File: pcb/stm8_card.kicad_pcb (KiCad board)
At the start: 2 copper layers, 101.9 x 50.9 mm, 22 parts, among them J1 DEBUG HEADER, SW1 TL59AF100Q, SW2 TL59AF100Q, SW3 TL59AF100Q, SW4 TL3302AF260QG, U1 ER-OLED0.91-7, U2 STM8S103F3

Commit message: pcb small edits
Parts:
- moved C8 2.00 mm to (261.5, 107.0)
- moved R1 2.00 mm to (229.0, 107.0)
- moved R3 2.00 mm to (251.5, 107.0)
- moved R4 2.00 mm to (254.0, 107.0), turned to 270 degrees
- moved R5 2.00 mm to (256.5, 107.0)
- moved R6 2.00 mm to (259.0, 107.0)
- moved C1 1.50 mm to (246.5, 107.0)
- moved C7 1.50 mm to (231.5, 107.0)
- moved R2 1.50 mm to (249.0, 107.0)
- moved C2 1.00 mm to (244.0, 107.0)
- moved C6 1.00 mm to (234.0, 107.0)
- moved C3 0.50 mm to (241.5, 107.0)
- moved C5 0.50 mm to (236.5, 107.0)
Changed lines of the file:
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@@
   )
   (module Capacitor_SMD:C_0805_2012Metric_Pad1.18x1.45mm_HandSolder (layer F.Cu)
-    (at 248 106.9625 90)
+    (at 246.5 107 90)
     (descr "Capacitor SMD 0805 (2012 Metric), square (rectangular) end terminal, IPC_7351 nominal with elongated pad for handsoldering. (Body size source: IPC-SM-782 page 76, https://www.pcb-3d.com/wordpress/wp-content/uploads/ipc-sm-782a_amendment_1_and_2.pdf, https://docs.google.com/spreadsheets/d/1BsfQQcO9C6DZCsRaXUlFlo91Tg2WpOkGARC1WS5S8t0/edit?usp=sharing), generated with kicad-footprint-generator")
     (tags "capacitor handsolder")
@@
   )
   (module Capacitor_SMD:C_0805_2012Metric_Pad1.18x1.45mm_HandSolder (layer F.Cu)
-    (at 245 106.9625 90)
+    (at 244 107 90)
     (descr "Capacitor SMD 0805 (2012 Metric), square (rectangular) end terminal, IPC_7351 nominal with elongated pad for handsoldering. (Body size source: IPC-SM-782 page 76, https://www.pcb-3d.com/wordpress/wp-content/uploads/ipc-sm-782a_amendment_1_and_2.pdf, https://docs.google.com/spreadsheets/d/1BsfQQcO9C6DZCsRaXUlFlo91Tg2WpOkGARC1WS5S8t0/edit?usp=sharing), generated with kicad-footprint-generator")
     (tags "capacitor handsolder")
@@
   )
   (module Capacitor_SMD:C_0805_2012Metric_Pad1.18x1.45mm_HandSolder (layer F.Cu)
-    (at 242 107.0375 90)
+    (at 241.5 107.0375 90)
     (descr "Capacitor SMD 0805 (2012 Metric), square (rectangular) end terminal, IPC_7351 nominal with elongated pad for handsoldering. (Body size source: IPC-SM-782 page 76, https://www.pcb-3d.com/wordpress/wp-content/uploads/ipc-sm-782a_amendment_1_and_2.pdf, https://docs.google.com/spreadsheets/d/1BsfQQcO9C6DZCsRaXUlFlo91Tg2WpOkGARC1WS5S8t0/edit?usp=sharing), generated with kicad-footprint-generator")
     (tags "capacitor handsolder")
@@
   )
   (module Capacitor_SMD:C_0805_2012Metric_Pad1.18x1.45mm_HandSolder (layer F.Cu)
-    (at 236 107.0375 270)
+    (at 236.5 107.0375 270)
     (descr "Capacitor SMD 0805 (2012 Metric), square (rectangular) end terminal, IPC_7351 nominal with elongated pad for handsoldering. (Body size source: IPC-SM-782 page 76, https://www.pcb-3d.com/wordpress/wp-content/uploads/ipc-sm-782a_amendment_1_and_2.pdf, https://docs.google.com/spreadsheets/d/1BsfQQcO9C6DZCsRaXUlFlo91Tg2WpOkGARC1WS5S8t0/edit?usp=sharing), generated with kicad-footprint-generator")
     (tags "capacitor handsolder")
@@
   )
   (module Capacitor_SMD:C_0805_2012Metric_Pad1.18x1.45mm_HandSolder (layer F.Cu)
-    (at 233 107.0375 270)
+    (at 234 107.0375 270)
     (descr "Capacitor SMD 0805 (2012 Metric), square (rectangular) end terminal, IPC_7351 nominal with elongated pad for handsoldering. (Body size source: IPC-SM-782 page 76, https://www.pcb-3d.com/wordpress/wp-content/uploads/ipc-sm-782a_amendment_1_and_2.pdf, https://docs.google.com/spreadsheets/d/1BsfQQcO9C6DZCsRaXUlFlo91Tg2WpOkGARC1WS5S8t0/edit?usp=sharing), generated with kicad-footprint-generator")
     (tags "capacitor handsolder")
@@
   )
   (module Capacitor_SMD:C_0805_2012Metric_Pad1.18x1.45mm_HandSolder (layer F.Cu)
-    (at 230 107.0375 270)
+    (at 231.5 107.0375 270)
     (descr "Capacitor SMD 0805 (2012 Metric), square (rectangular) end terminal, IPC_7351 nominal with elongated pad for handsoldering. (Body size source: IPC-SM-782 page 76, https://www.pcb-3d.com/wordpress/wp-content/uploads/ipc-sm-782a_amendment_1_and_2.pdf, https://docs.google.com/spreadsheets/d/1BsfQQcO9C6DZCsRaXUlFlo91Tg2WpOkGARC1WS5S8t0/edit?usp=sharing), generated with kicad-footprint-generator")
     (tags "capacitor handsolder")
@@
   )
   (module Capacitor_SMD:C_0805_2012Metric_Pad1.18x1.45mm_HandSolder (layer F.Cu)
-    (at 263.5 107 90)
+    (at 261.5 107 90)
     (descr "Capacitor SMD 0805 (2012 Metric), square (rectangular) end terminal, IPC_7351 nominal with elongated pad for handsoldering. (Body size source: IPC-SM-782 page 76, https://www.pcb-3d.com/wordpress/wp-content/uploads/ipc-sm-782a_amendment_1_and_2.pdf, https://docs.google.com/spreadsheets/d/1BsfQQcO9C6DZCsRaXUlFlo91Tg2WpOkGARC1WS5S8t0/edit?usp=sharing), generated with kicad-footprint-generator")
     (tags "capacitor handsolder")
@@
   )
   (module Resistor_SMD:R_0805_2012Metric_Pad1.20x1.40mm_HandSolder (layer F.Cu)
-    (at 227 107 90)
+    (at 229 107 90)
     (descr "Resistor SMD 0805 (2012 Metric), square (rectangular) end terminal, IPC_7351 nominal with elongated pad for handsoldering. (Body size source: IPC-SM-782 page 72, https://www.pcb-3d.com/wordpress/wp-content/uploads/ipc-sm-782a_amendment_1_and_2.pdf), generated with kicad-footprint-generator")
     (tags "resistor handsolder")
@@
   )
   (module Resistor_SMD:R_0805_2012Metric_Pad1.20x1.40mm_HandSolder (layer F.Cu)
-    (at 250.5 107 90)
+    (at 249 107 90)
     (descr "Resistor SMD 0805 (2012 Metric), square (rectangular) end terminal, IPC_7351 nominal with elongated pad for handsoldering. (Body size source: IPC-SM-782 page 72, https://www.pcb-3d.com/wordpress/wp-content/uploads/ipc-sm-782a_amendment_1_and_2.pdf), generated with kicad-footprint-generator")
     (tags "resistor handsolder")
@@
   )
   (module Resistor_SMD:R_0805_2012Metric_Pad1.20x1.40mm_HandSolder (layer F.Cu)
-    (at 253.5 107 90)
+    (at 251.5 107 90)
     (descr "Resistor SMD 0805 (2012 Metric), square (rectangular) end terminal, IPC_7351 nominal with elongated pad for handsoldering. (Body size source: IPC-SM-782 page 72, https://www.pcb-3d.com/wordpress/wp-content/uploads/ipc-sm-782a_amendment_1_and_2.pdf), generated with kicad-footprint-generator")
     (tags "resistor handsolder")
@@
   )
   (module Resistor_SMD:R_0805_2012Metric_Pad1.20x1.40mm_HandSolder (layer F.Cu)
-    (at 256 107 90)
-    (descr "Resistor SMD 0805 (2012 Metric), square (rectangular) end terminal, IPC_7351 nominal with elongated pad for handsoldering. (Body size source: IPC-SM-782 page 72, https://www.pcb-3d.com/wordpress/wp-content/uploads/ipc-sm-782a_amendment_1_and_2.pdf), generated with kicad-footprint-generator")
-    (tags "resistor handsolder")
-    (attr smd)
-    (fp_text reference R4 (at 3 0 180) (layer F.SilkS)
+    (at 254 107 270)
+    (descr "Resistor SMD 0805 (2012 Metric), square (rectangular) end terminal, IPC_7351 nominal with elongated pad for handsoldering. (Body size source: IPC-SM-782 page 72, https://www.pcb-3d.com/wordpress/wp-content/uploads/ipc-sm-782a_amendment_1_and_2.pdf), generated with kicad-footprint-generator")
+    (tags "resistor handsolder")
+    (attr smd)
+    (fp_text reference R4 (at -3 0 180) (layer F.SilkS)
       (effects (font (size 1 1) (thickness 0.15)))
     )
@@
       (effects (font (size 0.5 0.5) (thickness 0.08)))
     )
-    (pad 1 smd roundrect (at -1 0 90) (size 1.2 1.4) (layers F.Cu F.Paste F.Mask) (roundrect_rratio 0.208333)
-      (net 1 GND))
-    (pad 2 smd roundrect (at 1 0 90) (size 1.2 1.4) (layers F.Cu F.Paste F.Mask) (roundrect_rratio 0.208333)
+    (pad 1 smd roundrect (at -1 0 270) (size 1.2 1.4) (layers F.Cu F.Paste F.Mask) (roundrect_rratio 0.208333)
+      (net 1 GND))
+    (pad 2 smd roundrect (at 1 0 270) (size 1.2 1.4) (layers F.Cu F.Paste F.Mask) (roundrect_rratio 0.208333)
       (net 20 btn0))
     (model ${KISYS3DMOD}/Resistor_SMD.3dshapes/R_0805_2012Metric.wrl
@@
   )
   (module Resistor_SMD:R_0805_2012Metric_Pad1.20x1.40mm_HandSolder (layer F.Cu)
-    (at 258.5 107 270)
+    (at 256.5 107 270)
     (descr "Resistor SMD 0805 (2012 Metric), square (rectangular) end terminal, IPC_7351 nominal with elongated pad for handsoldering. (Body size source: IPC-SM-782 page 72, https://www.pcb-3d.com/wordpress/wp-content/uploads/ipc-sm-782a_amendment_1_and_2.pdf), generated with kicad-footprint-generator")
     (tags "resistor handsolder")
@@
   )
   (module Resistor_SMD:R_0805_2012Metric_Pad1.20x1.40mm_HandSolder (layer F.Cu)
-    (at 261 107 270)
-    (descr "Resistor SMD 0805 (2012 Metric), square (rectangular) end terminal, IPC_7351 nominal with elongated pad for handsoldering. (Body size source: IPC-SM-782 page 72, https://www.pcb-3d.com/wordpress/wp-content/uploads/ipc-sm-782a_amendment_1_and_2.pdf), generated with kicad-footprint-generator")
-    (tags "resistor handsolder")
+    (at 259 107 270)
+    (descr "Resistor SMD 0805 (2012 Metric), square (rectangular) end terminal, IPC_7351 nominal with elongated pad for handsoldering. (Body size source: IPC-SM-782 page 72, https://www.pcb-3d.com/wordpress/wp-content/uploads/ipc-sm-782a_amendment_1_and_2.pdf), generated with kicad-footprint-generator")
+    (tags "resistor handsolder")

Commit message: pcb technically finished I think?
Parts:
- moved C7 20.0 mm to (251.5, 106.0)
- moved C1 16.0 mm to (230.5, 106.0)
- moved R2 16.0 mm to (234.0, 112.5)
- moved R3 15.0 mm to (237.5, 112.5)
- moved R4 14.1 mm to (241.0, 112.5)
- moved C6 14.0 mm to (248.0, 106.0)
- moved R5 13.2 mm to (244.5, 112.5)
- moved R6 12.3 mm to (248.0, 112.5)
- moved C8 11.4 mm to (251.5, 112.5)
- moved C2 10.0 mm to (234.0, 106.0)
- moved C5 8.07 mm to (244.5, 106.0)
- moved R1 5.70 mm to (230.5, 112.5)
- moved C3 4.13 mm to (237.5, 106.0)
- moved C4 2.25 mm to (241.0, 106.0)
- moved J1 1.22 mm to (272.0, 106.0)
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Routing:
- net 3v3: track 0.00 -> 188.7 mm, vias 0 -> 2
- net Net-(C7-Pad2): track 0.00 -> 186.9 mm, vias 0 -> 2
- net btn0: track 0.00 -> 159.3 mm, vias 0 -> 2
- net btn1: track 0.00 -> 145.0 mm, vias 0 -> 2
- net NRST: track 0.00 -> 142.7 mm, vias 0 -> 2
- net btn2: track 0.00 -> 131.5 mm, vias 0 -> 2
- net Net-(R1-Pad1): track 0.00 -> 78.5 mm, vias 0 -> 2
- net SDA: track 0.00 -> 77.2 mm, vias 0 -> 3
- net SCL: track 0.00 -> 71.0 mm, vias 0 -> 3
- net GND: track 0.00 -> 69.8 mm, vias 0 -> 9
- net Net-(C2-Pad2): track 0.00 -> 48.3 mm, vias 0 -> 2
- net Net-(C6-Pad2): track 0.00 -> 34.9 mm, vias 0 -> 2
- net Net-(C1-Pad2): track 0.00 -> 33.8 mm, vias 0 -> 2
- net Net-(C1-Pad1): track 0.00 -> 32.9 mm
- net Net-(C4-Pad1): track 0.00 -> 27.9 mm, vias 0 -> 2
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- added copper zone on B.Cu, net GND
- added copper zone on F.Cu, net GND

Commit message: pcb more work on card
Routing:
- net Net-(C7-Pad2): track 186.9 -> 41.2 mm
- net GND: track 69.8 -> 152.0 mm
- net btn1: track 145.0 -> 157.1 mm, vias 2 -> 1
- net btn0: track 159.3 -> 170.7 mm, vias 2 -> 1
- net btn2: track 131.5 -> 141.4 mm, vias 2 -> 1
- net 3v3: track 188.7 -> 191.0 mm
- removed copper zone on B.Cu, net GND
- removed copper zone on F.Cu, net GND
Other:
- board text added: "A moderately humorous techie."
- board text added: "Embedded Linux Hardware Design Systems Programming C Ruby Git Emacs Lisp VHDL Nginx Hugo"
- board text added: "Richard Sent"
- board text added: "richard@freakingpenguin.com"

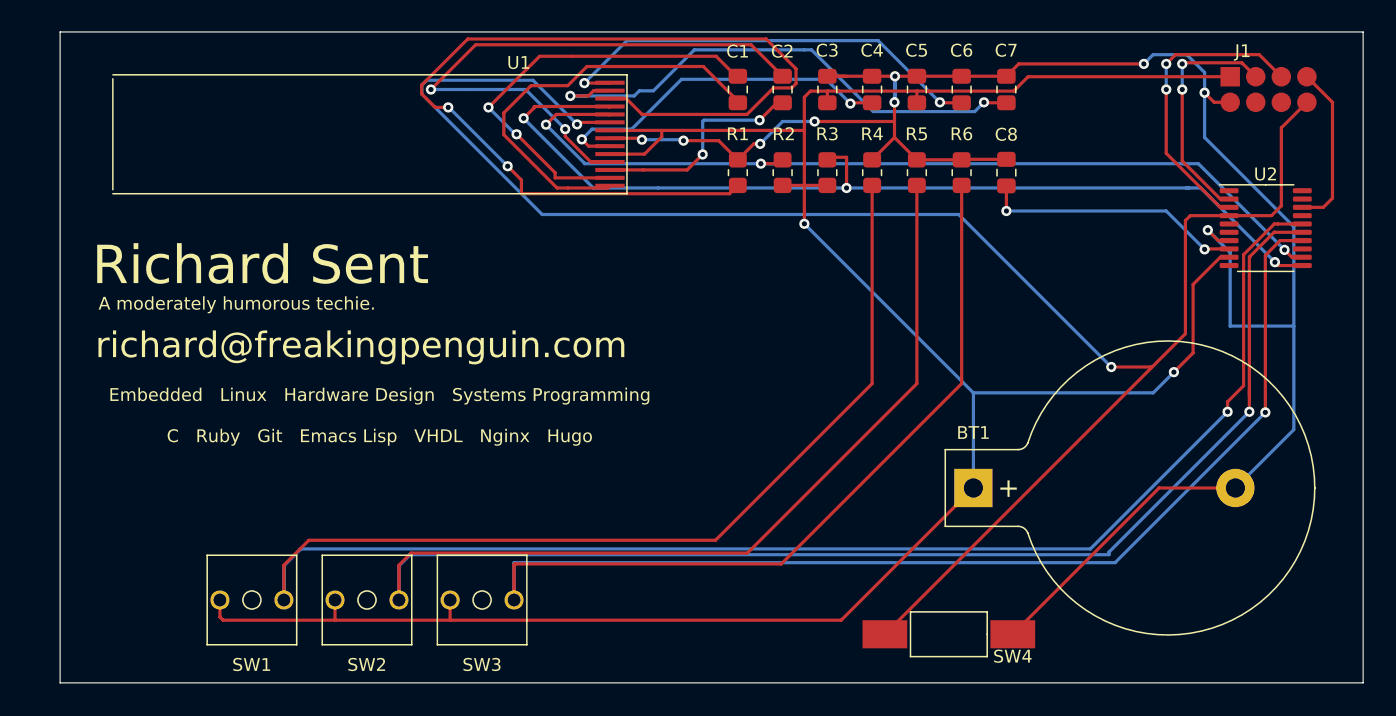
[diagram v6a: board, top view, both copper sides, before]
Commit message: pcb readded ground planes
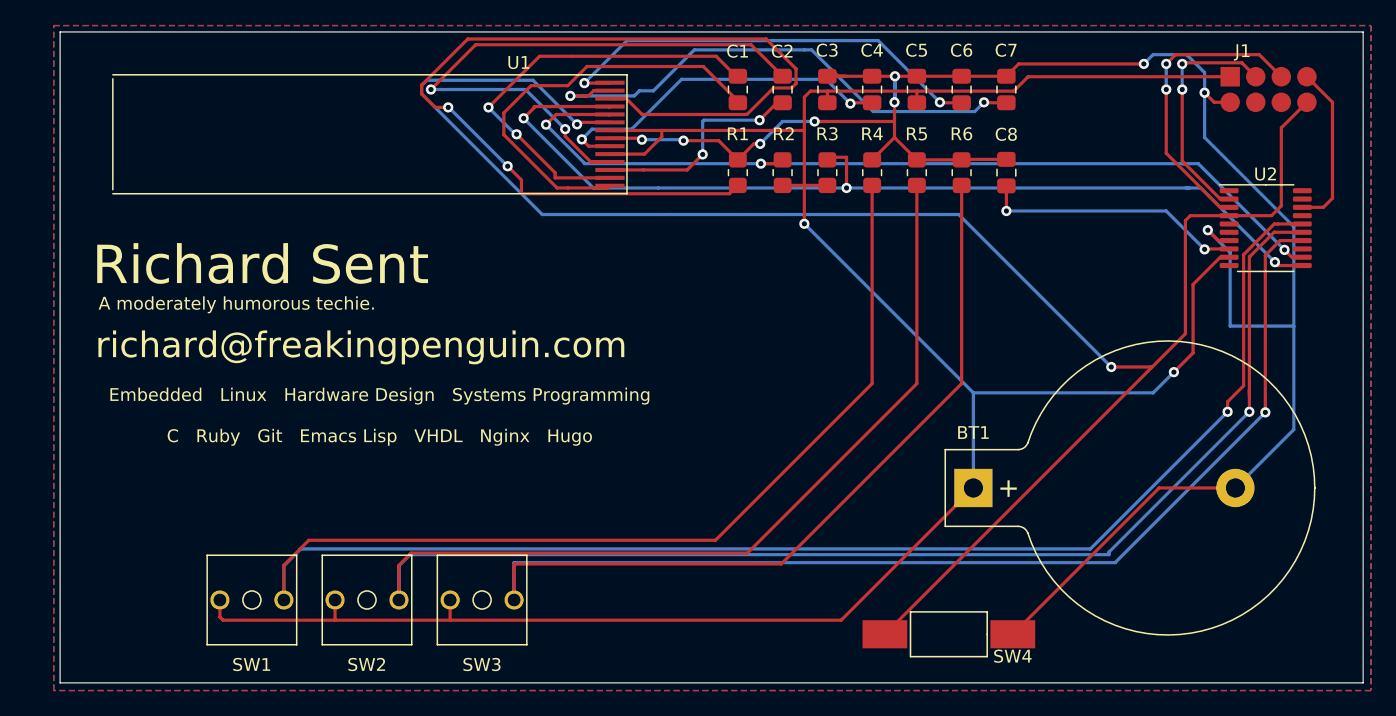
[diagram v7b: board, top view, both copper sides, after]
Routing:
- added copper zone on B.Cu, net GND
- added copper zone on F.Cu, net GND
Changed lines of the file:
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@@
   (page A4)
   (layers
-    (0 F.Cu signal)
+    (0 F.Cu signal hide)
     (31 B.Cu signal)
     (32 B.Adhes user)
@@
   (segment (start 213 145.92) (end 213 143.2) (width 0.25) (layer F.Cu) (net 22))
   (segment (start 213 143.1) (end 213.1 143.1) (width 0.25) (layer F.Cu) (net 22))
+  (zone (net 1) (net_name GND) (layer F.Cu) (hatch edge 0.508)
+    (connect_pads (clearance 0.508))
+    (min_thickness 0.254)
+    (fill yes (arc_segments 32) (thermal_gap 0.508) (thermal_bridge_width 0.508))
+    (polygon
+      (pts
+        (xy 280 153) (xy 177 153) (xy 177 101) (xy 280 101)
+      )
+    )
+  )
+  (zone (net 1) (net_name GND) (layer B.Cu) (hatch edge 0.508)
+    (connect_pads (clearance 0.508))
+    (min_thickness 0.254)
+    (fill yes (arc_segments 32) (thermal_gap 0.508) (thermal_bridge_width 0.508))
+    (polygon
+      (pts
+        (xy 280 153) (xy 177 153) (xy 177 101) (xy 280 101)
+      )
+    )
+  )
 )
